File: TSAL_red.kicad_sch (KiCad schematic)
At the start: 35 parts, among them U1 OPA355NA, U17 TBA1-0511E, U4 SFH617A-1X007T, U5 NE555D

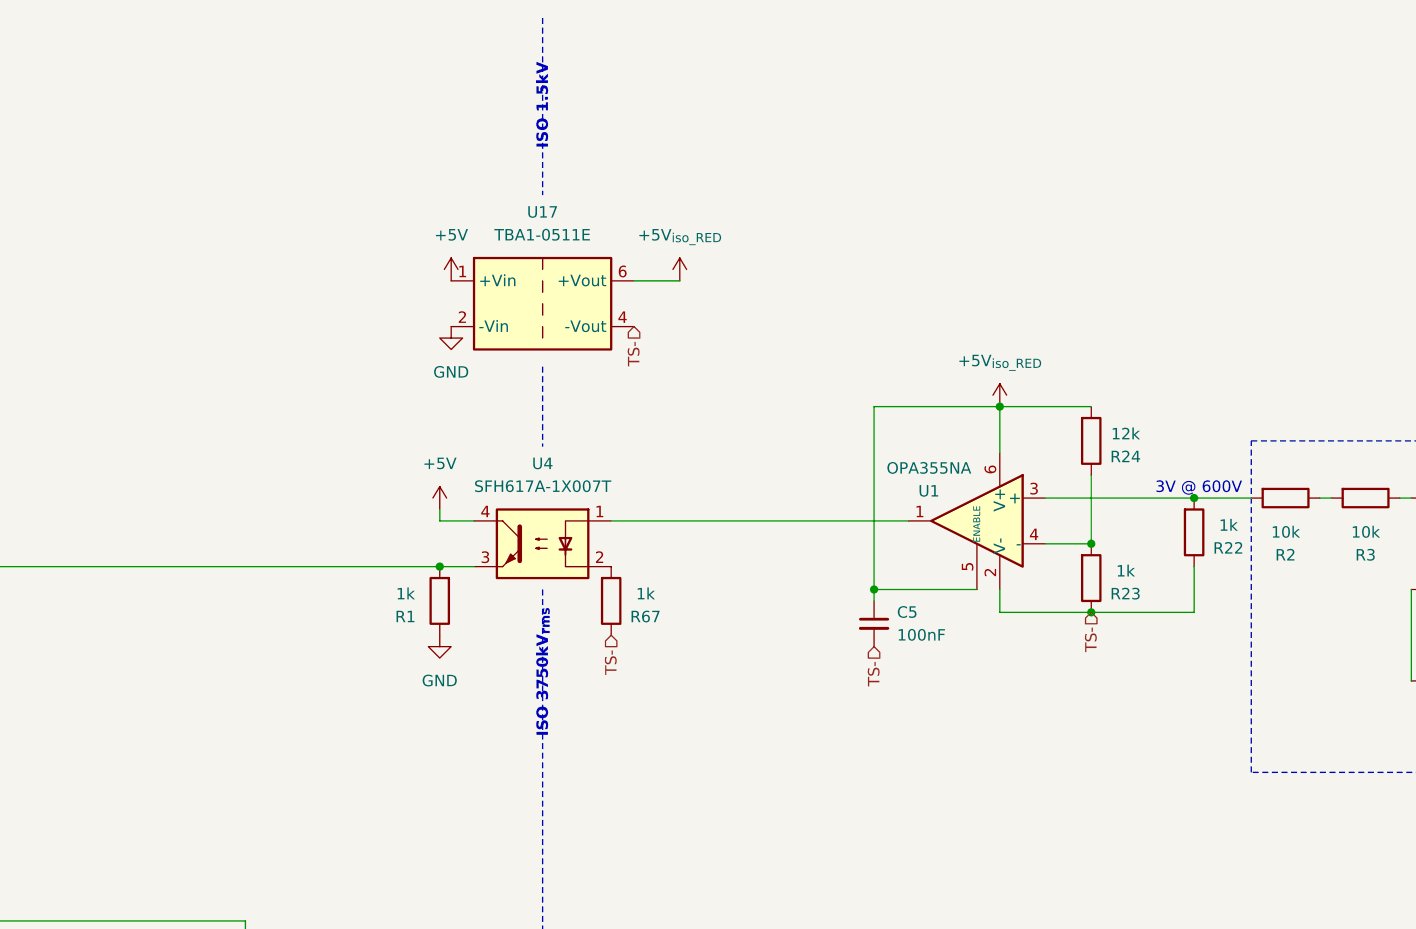
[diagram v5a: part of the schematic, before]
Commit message: Added decoupling Caps
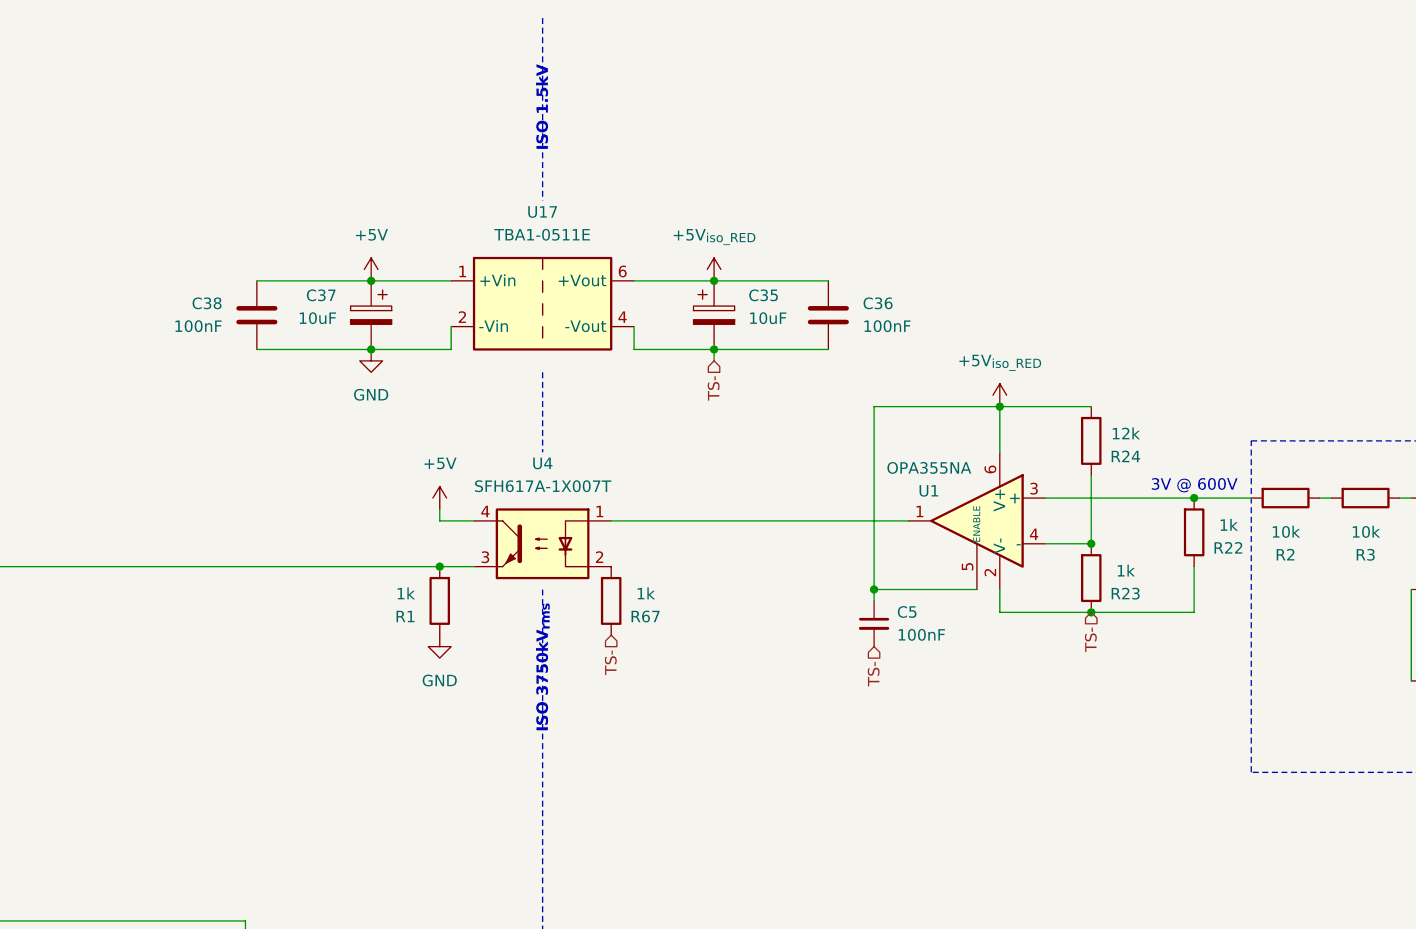
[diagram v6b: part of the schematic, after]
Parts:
- added C35, C37: 10uF, symbol Device:C_Polarized
- added C36, C38: 100nF, symbol Device:C
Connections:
- net +5V: now also C37.1, C38.1
- net +5V_{iso_RED}: now also C35.1, C36.1
- net GND: now also C37.2, C38.2
- net TS-: now also C35.2, C36.2

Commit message: Added Rules
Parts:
- added C2: 100nF, Capacitor_SMD:C_0603_1608Metric, symbol Device:C
- added Q7: NMOS, symbol Simulation_SPICE:NMOS
- added R82: 200R, Resistor_SMD:R_0603_1608Metric, symbol Device:R
- added R83: 10k, Resistor_SMD:R_0603_1608Metric, symbol Device:R
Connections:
- net +5V: now also C2.1
- net GND: now also C2.2, Q7.3 (S), R83.1
- net TSAL_RED_OUT: now also Q7.1 (D)
- net at U5.3 (Q): now also R82.1; no longer R27.2
- new net: Q7.2 (G), R82.2, R83.2
- new net +24V: R27.2
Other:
- note added: "LVS"
- note added: "TS VOLTAGE AREA"
- moved on the sheet: C6, C7, R25, R26, U5

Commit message: Submission Ready. ESF 15.07.24
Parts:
- removed R10, R11, R12, R13, R14, R15, R16, R17, R18, R19, R20, R21, R8, R9: 10k, Resistor_SMD:R_0603_1608Metric, symbol Device:R
- R2, R3, R4, R5, R6, R7: value 10k -> 52k3; footprint Resistor_SMD:R_0603_1608Metric -> Resistor_SMD:R_0805_2012Metric; Cost (none) -> 0.05; Mouser (none) -> 603-RT0805DRD0752K3L
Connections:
- net TS+: now also R7.1
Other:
- note added: "Resistor Datasheet"
